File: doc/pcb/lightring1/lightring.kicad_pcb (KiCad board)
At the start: 2 copper layers, 44 x 44 mm, 98 parts, among them SW1 SW_SPST, SW2 SW_SPST, U1 STM32G070RBT, Y1 Crystal

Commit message: finished PCB
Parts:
- added D43: LED, lightring:LR_LED, F.Cu at (164.5, 83.8)
- added J1: Conn_01x05_Female, Connector_PinHeader_1.27mm:PinHeader_1x05_P1.27mm_Vertical, F.Cu at (176.2, 72.5)
- added R44: R, lightring:LR_RES, B.Cu at (158.8, 74.3)
- moved R43 4.49 mm to (167.5, 74.6)
- moved C1 3.45 mm to (159.5, 84.0)
- moved C5 3.45 mm to (161.1, 84.0)
- moved C2 3.22 mm to (163.8, 75.5)
- moved C6 3.22 mm to (163.8, 77.0)
- moved C7 3.22 mm to (163.8, 72.5)
- moved C8 3.22 mm to (163.8, 74.0)
- moved BT1 0.22 mm to (167.1, 89.6)
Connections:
- U1 pad 1: M27 -> M23
- U1 pad 10: M25 -> Net-(U1-Pad10)
- U1 pad 11: M24 -> Net-(U1-Pad11)
- U1 pad 13: M23 -> Net-(U1-Pad13)
- U1 pad 14: H9 -> Net-(U1-Pad14)
- U1 pad 2: M26 -> H9
- U1 pad 31: H4 -> M10
- U1 pad 32: M10 -> H4
- U1 pad 45: M2 -> SWDIO
- U1 pad 46: M1 -> SWCLK
- U1 pad 49: Net-(U1-Pad49) -> M1
- U1 pad 50: Net-(U1-Pad50) -> M2
- U1 pad 51: Net-(U1-Pad51) -> M29
- U1 pad 52: M29 -> M28
- U1 pad 53: M28 -> H11
- U1 pad 54: Net-(U1-Pad54) -> M27
- U1 pad 55: H10 -> M26
- U1 pad 56: Net-(U1-Pad56) -> M25
- U1 pad 57: Net-(U1-Pad57) -> H10
- U1 pad 58: Net-(U1-Pad58) -> WORK
- U1 pad 64: H11 -> M24
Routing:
- net GND: track 0.00 -> 310.8 mm, vias 0 -> 13
- net VCC: track 0.00 -> 52.7 mm, vias 0 -> 3
- net SET: track 0.00 -> 36.0 mm, vias 0 -> 1
- net M20: track 0.00 -> 31.2 mm, vias 0 -> 2
- net M17: track 0.00 -> 26.9 mm
- net M19: track 0.00 -> 26.7 mm
- net H8: track 0.00 -> 26.4 mm
- net M18: track 0.00 -> 25.9 mm
- net M15: track 0.00 -> 24.1 mm
- net M16: track 0.00 -> 23.4 mm
- net M8: track 0.00 -> 23.4 mm
- net M11: track 0.00 -> 23.2 mm
- net M13: track 0.00 -> 23.0 mm
- net M12: track 0.00 -> 22.9 mm
- net H7: track 0.00 -> 22.6 mm
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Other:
- outline, holes or cut-outs redrawn
- net class Default: clearance 0.2 -> 0.18
- rule trace_clearance: 0.2 -> 0.18
- board text added: "lightring"

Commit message: v2 base board
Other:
- board text added: "ARM Cortex"
- board text added: "WAKE^"
- board text added: "^SET"
- board text added: "crystal"
- board text added: "lightring v0.1"

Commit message: v0.2 board
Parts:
- removed C3: 105, lightring:LC_CAP
- removed SW1: SW_SPST, Button_Switch_SMD:Panasonic_EVQPUJ_EVQPUA
- added C10: 100nF, Capacitor_SMD:C_0603_1608Metric, B.Cu at (174.4, 66.4)
- added C11: 2.2n, Capacitor_SMD:C_0603_1608Metric, B.Cu at (171.5, 80.6)
- added C12: 105, Capacitor_SMD:C_0603_1608Metric, B.Cu at (178.8, 70.5)
- added C9: 475, Capacitor_SMD:C_0603_1608Metric, B.Cu at (156.3, 68.4)
- added D44: LED, Diode_SMD:D_0603_1608Metric, B.Cu at (151.9, 72.2)
- added J2: USB_B_Micro, Connector_USB:USB_Micro-B_Molex_47346-0001, B.Cu at (150.8, 79.9)
- added J3: plate, lightring:touchplate, F.Cu at (174.1, 88.4)
- added R45: 12k, Resistor_SMD:R_0603_1608Metric, B.Cu at (159.1, 65.0)
- added R46: 100k, Resistor_SMD:R_0603_1608Metric, B.Cu at (166.6, 82.9)
- added R47: 1M, Resistor_SMD:R_0603_1608Metric, B.Cu at (172.7, 77.7)
- added R48: 470R, Resistor_SMD:R_0603_1608Metric, B.Cu at (161.5, 65.1)
- added R49: 10k, Resistor_SMD:R_0603_1608Metric, B.Cu at (169.0, 82.4)
- added U2: MCP73831-2-OT, Package_TO_SOT_SMD:SOT-23-5, B.Cu at (159.4, 68.5)
- added U3: AT42QT1012-T, Package_TO_SOT_SMD:SOT-23-6, B.Cu at (168.8, 79.5)
- added U4: LDK130-33_SOT23_SOT353, Package_TO_SOT_SMD:SOT-23-5, B.Cu at (174.7, 69.1)
- BT1: footprint Battery:BatteryHolder_Keystone_500 -> Resistor_SMD:R_1206_3216Metric; moved to B.Cu
- C1, C2, C4, C5, C6, C7, C8: footprint lightring:LC_CAP -> Capacitor_SMD:C_0603_1608Metric
- R43, R44: footprint lightring:LR_RES -> Resistor_SMD:R_0603_1608Metric
- moved BT1 28.8 mm to (164.6, 60.9), turned to 0 degrees
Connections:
- C2 pad 1: VCC -> +3V3
- C6 pad 1: VCC -> +3V3
- C7 pad 1: VCC -> +3V3
- C8 pad 1: VCC -> +3V3
- R43 pad 1: VCC -> +3V3
- U1 pad 14: Net-(U1-Pad14) -> TOUCH
- U1 pad 6: VCC -> +3V3
- U1 pad 7: VCC -> +3V3
- U1 pad 8: VCC -> +3V3
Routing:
- net GND: track 310.8 -> 371.2 mm, vias 13 -> 19
- net +3V3: track 0.00 -> 49.2 mm, vias 0 -> 1
- net WAKE: track 29.3 -> 2.68 mm, vias 1 -> 0
- net +5V: track 0.00 -> 23.7 mm, vias 0 -> 2
- net Net-(D44-Pad1): track 0.00 -> 15.6 mm
- net Net-(C11-Pad1): track 0.00 -> 13.8 mm
- net Net-(J2-Pad6): track 0.00 -> 12.6 mm
- net M20: track 31.2 -> 21.8 mm
- net Net-(J3-Pad1): track 0.00 -> 9.36 mm, vias 0 -> 1
- net H5: track 19.5 -> 28.1 mm, vias 0 -> 2
- net H8: track 26.4 -> 18.1 mm
- net TOUCH: track 0.00 -> 7.95 mm, vias 0 -> 1
- net M19: track 26.7 -> 19.2 mm
- net M14: track 22.6 -> 30.1 mm
- net M18: track 25.9 -> 19.5 mm
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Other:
- board text added: "Mk1"
- board text added: "WAKE"
- board text added: "lightring v0.2"
- board text removed: "WAKE^"
- board text removed: "lightring v0.1"

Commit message: initial program
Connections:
- net WAKE renamed Net-(U1-Pad41)
- U1 pad 3: XTAL1 -> Net-(U1-Pad3)
- U1 pad 4: XTAL2 -> XTAL1
- U1 pad 5: (no net) -> XTAL2
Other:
- board text added: "lightring v0.3"
- board text removed: "lightring v0.2"

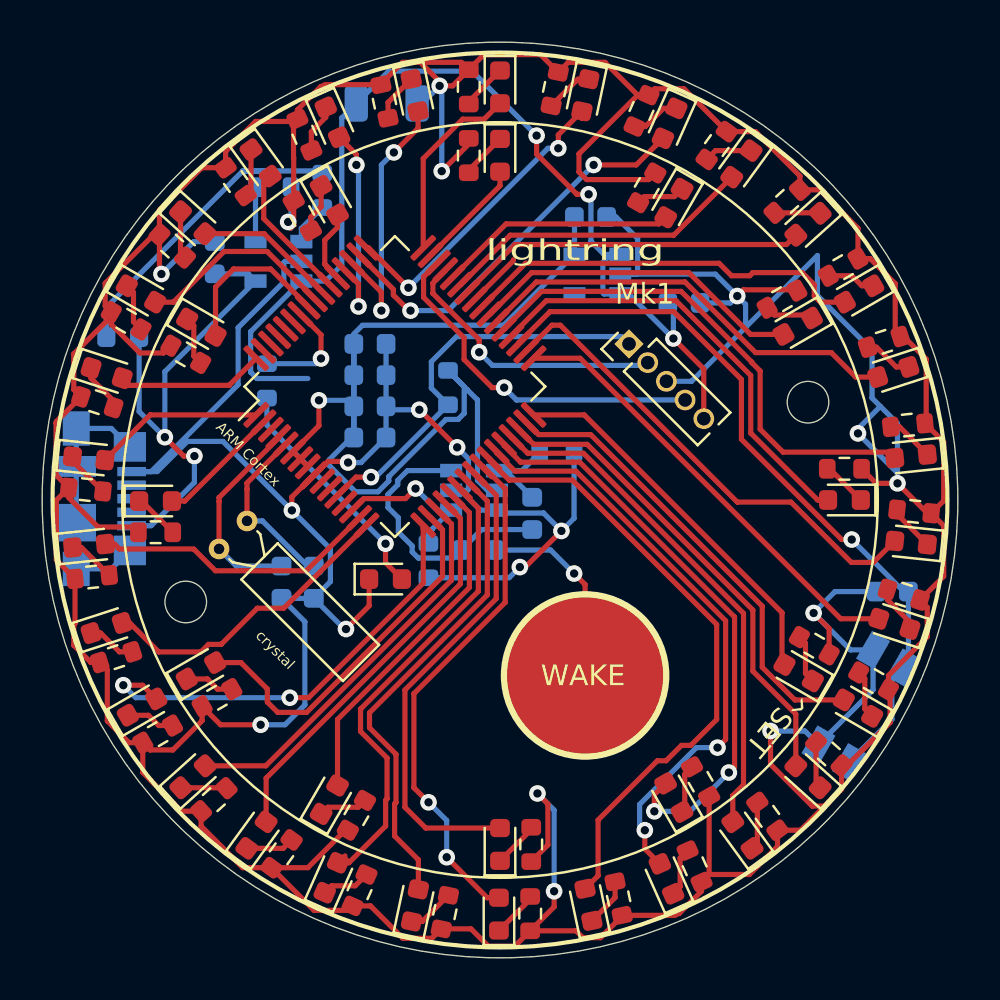
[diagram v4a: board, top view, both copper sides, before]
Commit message: silks corrections
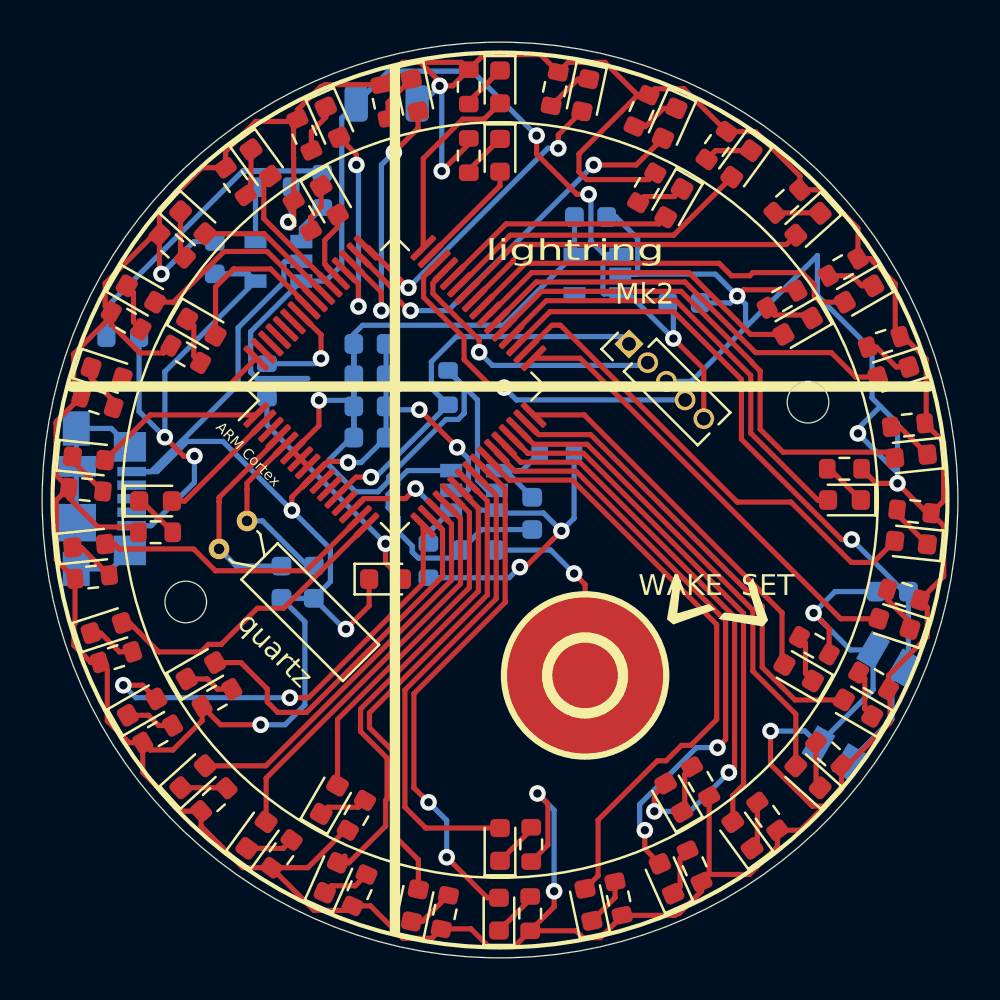
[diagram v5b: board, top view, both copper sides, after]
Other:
- board text added: "Mk2"
- board text added: "WAKE SET"
- board text added: "^"
- board text added: "quartz"
- board text removed: "Mk1"
- board text removed: "WAKE"
- board text removed: "^SET"
- board text removed: "crystal"
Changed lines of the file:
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@@
-(kicad_pcb (version 20171130) (host pcbnew 5.1.8-1.fc33)
+(kicad_pcb (version 20171130) (host pcbnew "(5.1.4)-1")
   (general
     (thickness 1.6)
-    (drawings 32)
+    (drawings 36)
     (tracks 861)
     (zones 0)
@@
     (pad_to_mask_clearance 0)
     (aux_axis_origin 0 0)
-    (visible_elements FFFFFF7F)
+    (visible_elements 7FFFFFFF)
     (pcbplotparams
       (layerselection 0x010fc_ffffffff)
@@
     )
   )
+  (gr_circle (center 174.08906 88.4301) (end 175.91456 88.4301) (layer F.SilkS) (width 0.5))
+  (gr_line (start 164.95 100.7) (end 164.95 59.3) (layer F.SilkS) (width 0.5))
+  (gr_line (start 149.4 74.55) (end 190.6 74.55) (layer F.SilkS) (width 0.5))
+  (gr_text ^ (at 179.9 83.8 140) (layer F.SilkS)
+    (effects (font (size 5 3) (thickness 0.15)))
+  )
   (gr_text "lightring v0.3" (at 173.64 91.32) (layer B.SilkS)
     (effects (font (size 1 1) (thickness 0.15)) (justify mirror))
   )
-  (gr_text Mk1 (at 176.95 70.1) (layer F.SilkS)
+  (gr_text Mk2 (at 176.95 70.1) (layer F.SilkS)
     (effects (font (size 1 1) (thickness 0.15)))
   )
-  (gr_text WAKE (at 173.99 88.44) (layer F.SilkS)
+  (gr_text "WAKE  SET" (at 180.4 84.1) (layer F.SilkS)
     (effects (font (size 1 1) (thickness 0.15)))
   )
-  (gr_text ^SET (at 183.3 90.7 -130) (layer F.SilkS)
-    (effects (font (size 1 1) (thickness 0.15)))
+  (gr_text ^ (at 180.7 84.2 -130) (layer F.SilkS)
+    (effects (font (size 5 3) (thickness 0.15)))
   )
   (gr_text "ARM Cortex" (at 157.9 77.8 -45) (layer F.SilkS)
     (effects (font (size 0.5 0.5) (thickness 0.1)))
   )
-  (gr_text crystal (at 159.2 87.2 -45) (layer F.SilkS)
-    (effects (font (size 0.5 0.5) (thickness 0.1)))
+  (gr_text quartz (at 159.2 87.2 -45) (layer F.SilkS)
+    (effects (font (size 1 1) (thickness 0.15)))
   )
   (gr_text lightring (at 173.6 68) (layer F.SilkS)
@@
   (segment (start 157.325 83.175) (end 156.5 82.35) (width 0.25) (layer B.Cu) (net 3) (status 20))
   (segment (start 159.5 83.175) (end 157.325 83.175) (width 0.25) (layer B.Cu) (net 3) (status 10))
-  (segment (start 168.786054 70.360392) (end 170.646446 68.5) (width 0.25) (layer F.Cu) (net 117) (status 10))
-  (segment (start 170.646446 68.5) (end 170.646446 68.453554) (width 0.25) (layer F.Cu) (net 117))
+  (segment (start 159.346179 76.971841) (end 159.346179 77.007179) (width 0.25) (layer F.Cu) (net 3) (status 30))
+  (segment (start 159.346179 77.035463) (end 156.5 79.881642) (width 0.25) (layer F.Cu) (net 3))
+  (segment (start 156.5 79.881642) (end 156.5 80.07) (width 0.25) (layer F.Cu) (net 3))
+  (segment (start 159.346179 76.971841) (end 159.346179 77.035463) (width 0.25) (layer F.Cu) (net 3))
+  (segment (start 156.5 82.35) (end 156.5 80.07) (width 0.25) (layer F.Cu) (net 3))
   (via (at 186.9 81.9) (size 0.8) (drill 0.4) (layers F.Cu B.Cu) (net 4))
   (segment (start 189.4 84.4) (end 189.625 84.4) (width 0.25) (layer B.Cu) (net 4) (status 30))
@@
   (segment (start 158.584331 81.006497) (end 160.752834 83.175) (width 0.25) (layer B.Cu) (net 5) (status 20))
   (segment (start 157.843503 81.006497) (end 158.584331 81.006497) (width 0.25) (layer B.Cu) (net 5) (status 10))
-  (segment (start 159.346179 76.971841) (end 159.346179 77.007179) (width 0.25) (layer F.Cu) (net 3) (status 30))
-  (segment (start 159.346179 77.035463) (end 156.5 79.881642) (width 0.25) (layer F.Cu) (net 3))
-  (segment (start 156.5 79.881642) (end 156.5 80.07) (width 0.25) (layer F.Cu) (net 3))
-  (segment (start 159.346179 76.971841) (end 159.346179 77.035463) (width 0.25) (layer F.Cu) (net 3))
-  (segment (start 156.5 82.35) (end 156.5 80.07) (width 0.25) (layer F.Cu) (net 3))
   (segment (start 157.843503 79.181623) (end 157.843503 79.476497) (width 0.25) (layer F.Cu) (net 5))
   (segment (start 157.843503 79.476497) (end 157.843503 81.006497) (width 0.25) (layer F.Cu) (net 5))
@@
   (segment (start 160.45198 66.95302) (end 161.46 65.945) (width 0.25) (layer B.Cu) (net 115))
   (segment (start 160.45198 67.58174) (end 160.45198 66.95302) (width 0.25) (layer B.Cu) (net 115))
+  (segment (start 168.786054 70.360392) (end 170.646446 68.5) (width 0.25) (layer F.Cu) (net 117) (status 10))
+  (segment (start 170.646446 68.5) (end 170.646446 68.453554) (width 0.25) (layer F.Cu) (net 117))
 )
